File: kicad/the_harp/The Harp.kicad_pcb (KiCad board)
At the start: 4 copper layers, 56 x 94.5 mm, 181 parts, among them J401 PJ-063AH, J402 NMJ6HCD2, J403 NMJ6HCD2, J404 NMJ6HCD2, J405 Bypass FSW, J406 NMJ6HCD2, J407 Hold FSW, K401 G6K-2F-Y, Q401 2N7002, Q402 2N7002, Q403 2N7002, SW101 100-DP6, SW102 100-DP6, SW103 100-DP6, U201 STM32H750VBT6, U301 TPS54202DDC, U302 NCP718ASN500T1G, U401 MCP6001T-I/OT, U501 OPA2348AIDR, U601 THS4522IPW, U701 OPA2365AIDR, U702 OPA1688IDR, Y201 25MHz 9pF

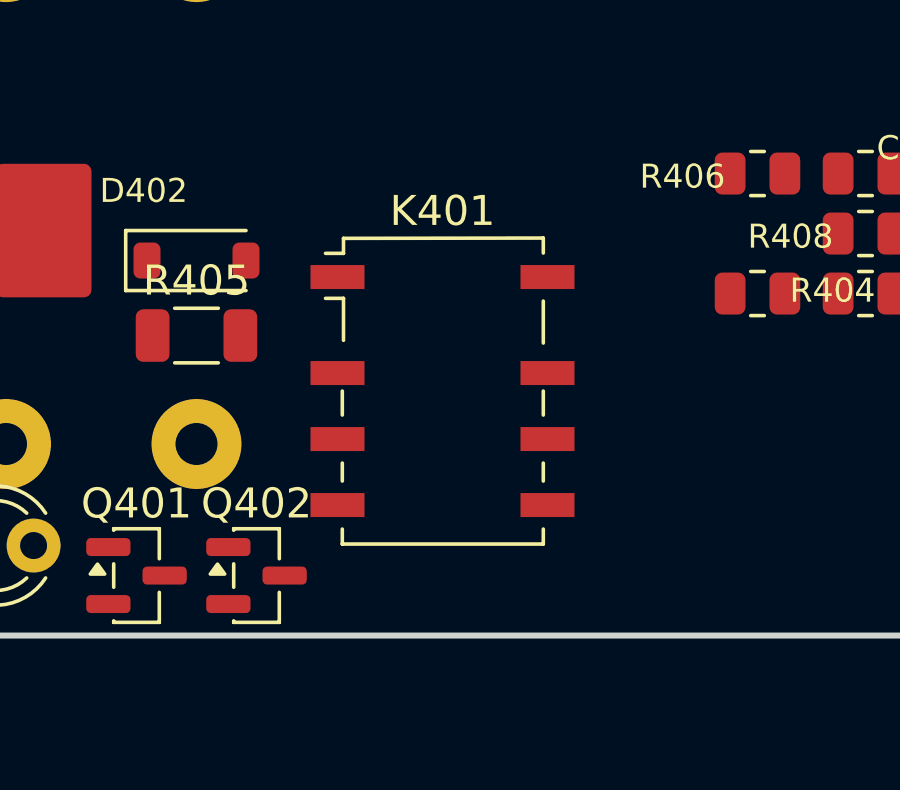
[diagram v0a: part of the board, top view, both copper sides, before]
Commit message: Move K401 out from under the OLED module
K401 from PCB (143.4, 134.85) to (143.9, 137.0), face (-4.6, -32.0): 2.15 mm
towards the heel and 0.5 mm right. Its courtyard now ends 0.5 mm short of the
module edge (Y -26.25), 0.12 mm clear of Q402 and 0.75 mm from the board edge;
a straight 2.5 mm move would have overlapped Q402. No tracks to move (board
unrouted). Drawing and docs updated.

Co-Authored-By: Claude Opus 5.5 <noreply@anthropic.com>
Claude-Session: https://claude.ai/code/session_016hDejPHPgG8auBLMyByYZK
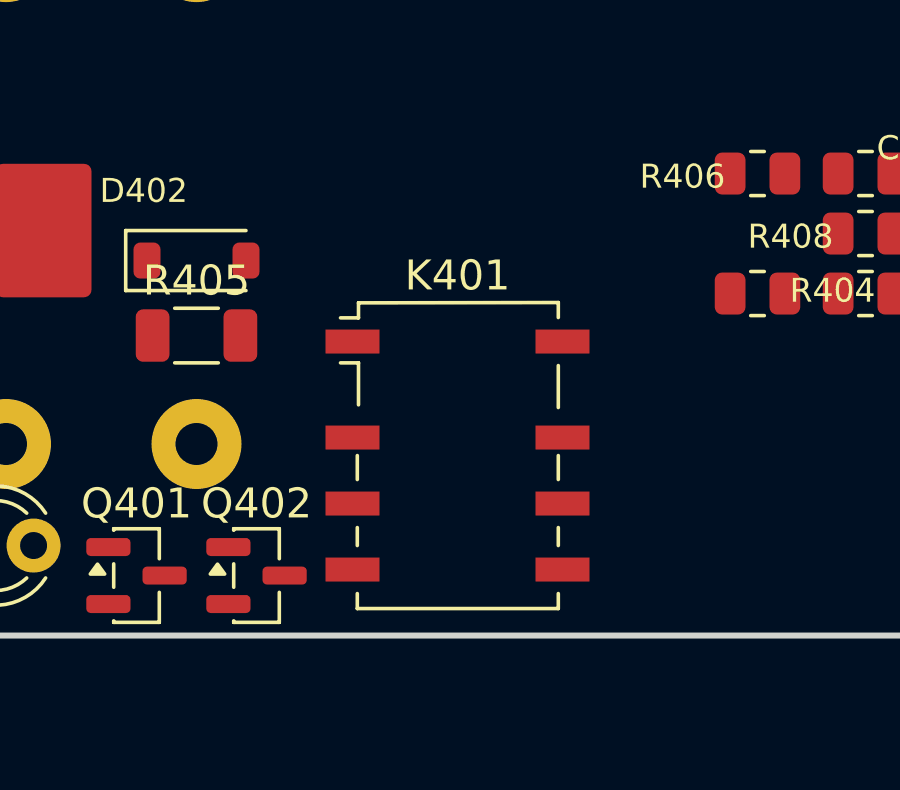
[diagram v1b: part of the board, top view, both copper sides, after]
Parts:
- moved K401 2.21 mm to (143.9, 137.0)
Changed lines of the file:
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@@
 	(footprint "Relay_SMD:Relay_DPDT_Omron_G6K-2F-Y"
 		(layer "F.Cu")
-		(at 143.4 134.85)
+		(at 143.9 137)
 		(descr "Omron G6K-2F-Y relay package http://omronfs.omron.com/en_US/ecb/products/pdf/en-g6k.pdf")
 		(tags "Omron G6K-2F-Y relay")

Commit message: Place J408 on the PCB for the OLED lead
JST SH SM04B-SRSS-TB footprint (KiCad library) added to the board at PCB
(125.0, 122.5), rotation 90, face (-23.5, -17.5): pads in a column at face
X -25.5, cable entry facing the module's pad end. Linked to the schematic
symbol (path /Controls and LEDs/J408) with nets GND, +3V3, OLED_SCL,
OLED_SDA, so Update PCB from Schematic keeps it. Courtyard 1.22 mm from the
board edge and 0.62 mm clear of J405. Drawing and docs updated.

Co-Authored-By: Claude Opus 5.5 <noreply@anthropic.com>
Claude-Session: https://claude.ai/code/session_016hDejPHPgG8auBLMyByYZK
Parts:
- added J408: OLED 0.91 128x32, Connector_JST:JST_SH_SM04B-SRSS-TB_1x04-1MP_P1.00mm_Horizontal, F.Cu at (125.0, 122.5)

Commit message: Sync the PCB to the schematic and park the new parts
Done by script (no KiCad in this session), the equivalent of Update PCB from
Schematic:
- removed D101-D112, R109-R118 (note LEDs) and R502/R503 (parked AINR)
- added 23 footprints: the stereo input parts (R607-R612, C611-C618,
  R720-R722, C708, C709, D407), C104, and IC501 / U202, which were missing
  from the board; library footprints cloned from this board or the
  Timekeeper's, rotation normalised, fresh UUIDs, linked to their symbols
- updated values and pad nets on 13 footprints (U601 channel B, U701B,
  IC501 inputs, ADC_L nets, J402 ring, U201 PB6/PB7 and freed PD0-PD11,
  R107/R108 now 4.7k pull-ups)
Checked: all 181 footprints match harp_spec.py pin by pin, every path
points at a schematic symbol. New parts are parked off-board at face X
132-160 beside the other parked groups.

Co-Authored-By: Claude Opus 5.5 <noreply@anthropic.com>
Claude-Session: https://claude.ai/code/session_016hDejPHPgG8auBLMyByYZK
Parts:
- removed D101, D102, D103, D104, D105, D106, D107, D108, D109, D110, D111, D112: LED, LED_SMD:LED_0603_1608Metric
- removed R109, R110, R111, R112, R113, R114, R115, R116, R117, R118, R502, R503: 1k, Resistor_SMD:R_0603_1608Metric
- added C104: 100n, Capacitor_SMD:C_0603_1608Metric, F.Cu at (280.5, 80.0)
- added C611: 100p, Capacitor_SMD:C_0603_1608Metric, F.Cu at (280.5, 132.0)
- added C612: 100p, Capacitor_SMD:C_0603_1608Metric, F.Cu at (284.5, 132.0)
- added C613: 1n, Capacitor_SMD:C_0603_1608Metric, F.Cu at (288.5, 132.0)
- added C614: 1n, Capacitor_SMD:C_0603_1608Metric, F.Cu at (292.5, 132.0)
- added C615: 2.7n, Capacitor_SMD:C_0603_1608Metric, F.Cu at (296.5, 132.0)
- added C616: 100p, Capacitor_SMD:C_0603_1608Metric, F.Cu at (300.5, 132.0)
- added C617: 100p, Capacitor_SMD:C_0603_1608Metric, F.Cu at (304.5, 132.0)
- added C618: 100n, Capacitor_SMD:C_0603_1608Metric, F.Cu at (308.5, 132.0)
- added C708: 100n, Capacitor_SMD:C_1206_3216Metric, F.Cu at (293.5, 115.0)
- added C709: 220p, Capacitor_SMD:C_0603_1608Metric, F.Cu at (298.5, 115.0)
- added D407: PESD5V0U1BB,115, Diode_SMD:D_SOD-523, F.Cu at (280.5, 105.0)
- added IC501: AK4621EF, Audio_Module:SOP65P760X150-30N, F.Cu at (288.5, 150.0)
- added R607: 1k, Resistor_SMD:R_0603_1608Metric, F.Cu at (280.5, 127.0)
- added R608: 1.05k, Resistor_SMD:R_0603_1608Metric, F.Cu at (284.5, 127.0)
- added R609: 620, Resistor_SMD:R_0603_1608Metric, F.Cu at (288.5, 127.0)
- added R610: 620, Resistor_SMD:R_0603_1608Metric, F.Cu at (292.5, 127.0)
- added R611: 40.2, Resistor_SMD:R_0603_1608Metric, F.Cu at (296.5, 127.0)
- added R612: 40.2, Resistor_SMD:R_0603_1608Metric, F.Cu at (300.5, 127.0)
- added R720: 1M, Resistor_SMD:R_0603_1608Metric, F.Cu at (280.5, 115.0)
- added R721: 1M, Resistor_SMD:R_0603_1608Metric, F.Cu at (284.5, 115.0)
- added R722: 49.9, Resistor_SMD:R_0603_1608Metric, F.Cu at (288.5, 115.0)
- added U202: W25Q128JVSIQ, Package_SO:SOIC-8_5.23x5.23mm_P1.27mm, F.Cu at (286.5, 95.0)
- R107, R108: value 1k -> 4.7k
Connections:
- net /Analog In and Out/U701B_OUT renamed /Analog In and Out/IN_BUF_OUT_R
- net ADC_N renamed ADC_L_N
- net ADC_P renamed ADC_L_P
- J402 pad R: GND -> IN_R
- R107 pad 1: NOTE_C -> +3V3
- R107 pad 2: /Controls and LEDs/NOTE_C_A -> OLED_SCL
- R108 pad 1: NOTE_Cs -> +3V3
- R108 pad 2: /Controls and LEDs/NOTE_Cs_A -> OLED_SDA
- U201 pad 55: NOTE_Gs -> unconnected-(U201-PD8-Pad55)
- U201 pad 56: NOTE_A -> unconnected-(U201-PD9-Pad56)
- U201 pad 57: NOTE_As -> unconnected-(U201-PD10-Pad57)
- U201 pad 58: NOTE_B -> unconnected-(U201-PD11-Pad58)
- U201 pad 81: NOTE_C -> unconnected-(U201-PD0-Pad81)
- U201 pad 82: NOTE_Cs -> unconnected-(U201-PD1-Pad82)
- U201 pad 83: NOTE_D -> unconnected-(U201-PD2-Pad83)
- U201 pad 84: NOTE_Ds -> unconnected-(U201-PD3-Pad84)
- U201 pad 85: NOTE_E -> unconnected-(U201-PD4-Pad85)
- U201 pad 86: NOTE_F -> unconnected-(U201-PD5-Pad86)
- U201 pad 87: NOTE_Fs -> unconnected-(U201-PD6-Pad87)
- U201 pad 88: NOTE_G -> unconnected-(U201-PD7-Pad88)
- U201 pad 92: unconnected-(U201-PB6-Pad92) -> OLED_SCL
- U201 pad 93: unconnected-(U201-PB7-Pad93) -> OLED_SDA
- U601 pad 10: unconnected-(U601B-OUTP-Pad10) -> /ADC Driver/FDB_OUTP
- U601 pad 11: unconnected-(U601B-OUTN-Pad11) -> /ADC Driver/FDB_OUTN
- U601 pad 5: GND -> +5V
- U601 pad 6: GND -> /ADC Driver/FDB_INP
- U601 pad 7: GND -> /ADC Driver/FDB_INN
- U601 pad 8: GND -> VCOM_B
- U701 pad 5: VCOM_A -> /Analog In and Out/IN_AC_R

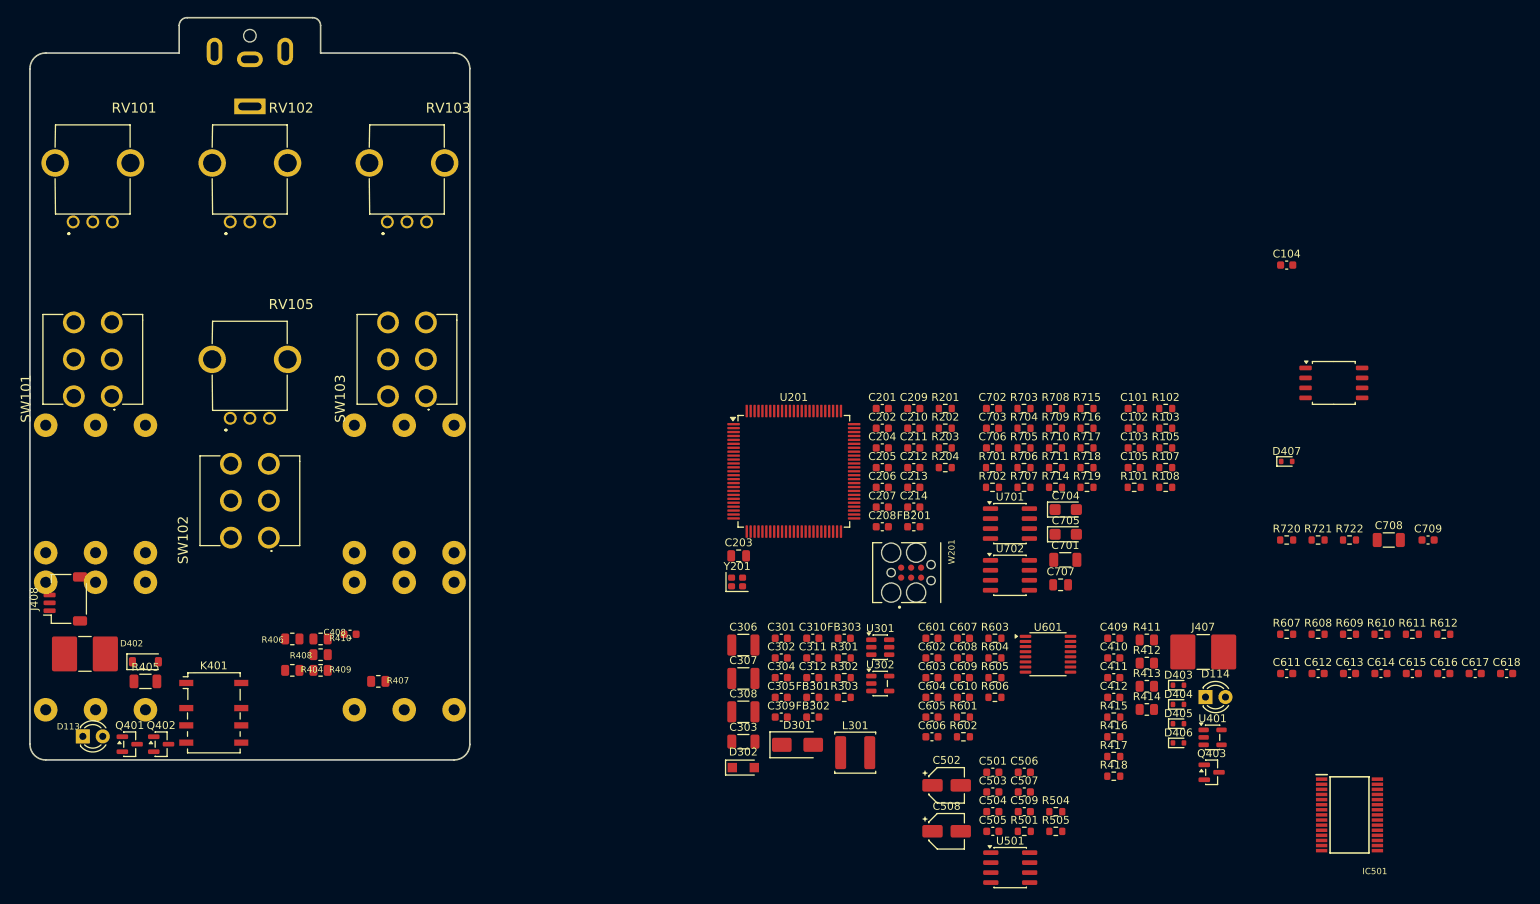
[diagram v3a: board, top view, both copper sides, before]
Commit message: Place every part on the board (scripted), Plan A go/no-go
All 181 footprints placed on the top side by a greedy, zoned placer
(scripts/pcb_placement/): no courtyard overlaps, everything inside the
outline, nothing tall under the OLED module, about 68 % courtyard fill.

The LQFP-100 fits in only one place, the lower centre between the lower
jacks' pin rows (0, -21.5), so the zoning was adapted round it: relay next
to IN, input buffers lower right, ADC driver left middle, codec and output
stages between the pot rows, buck and LDO in the top band. J408 moved to
(-21.75, -22.0): its first position sat on J403's rear pins.

Verdict in docs/pcb-plan.md "Placement": Plan A fits, but the right-channel
ADC driver network, the codec-to-MCU SAI lines and the input path need
rework by hand before routing. Placement drawing, OLED drawing, brief,
design report and READMEs updated.

Co-Authored-By: Claude Opus 5.5 <noreply@anthropic.com>
Claude-Session: https://claude.ai/code/session_016hDejPHPgG8auBLMyByYZK
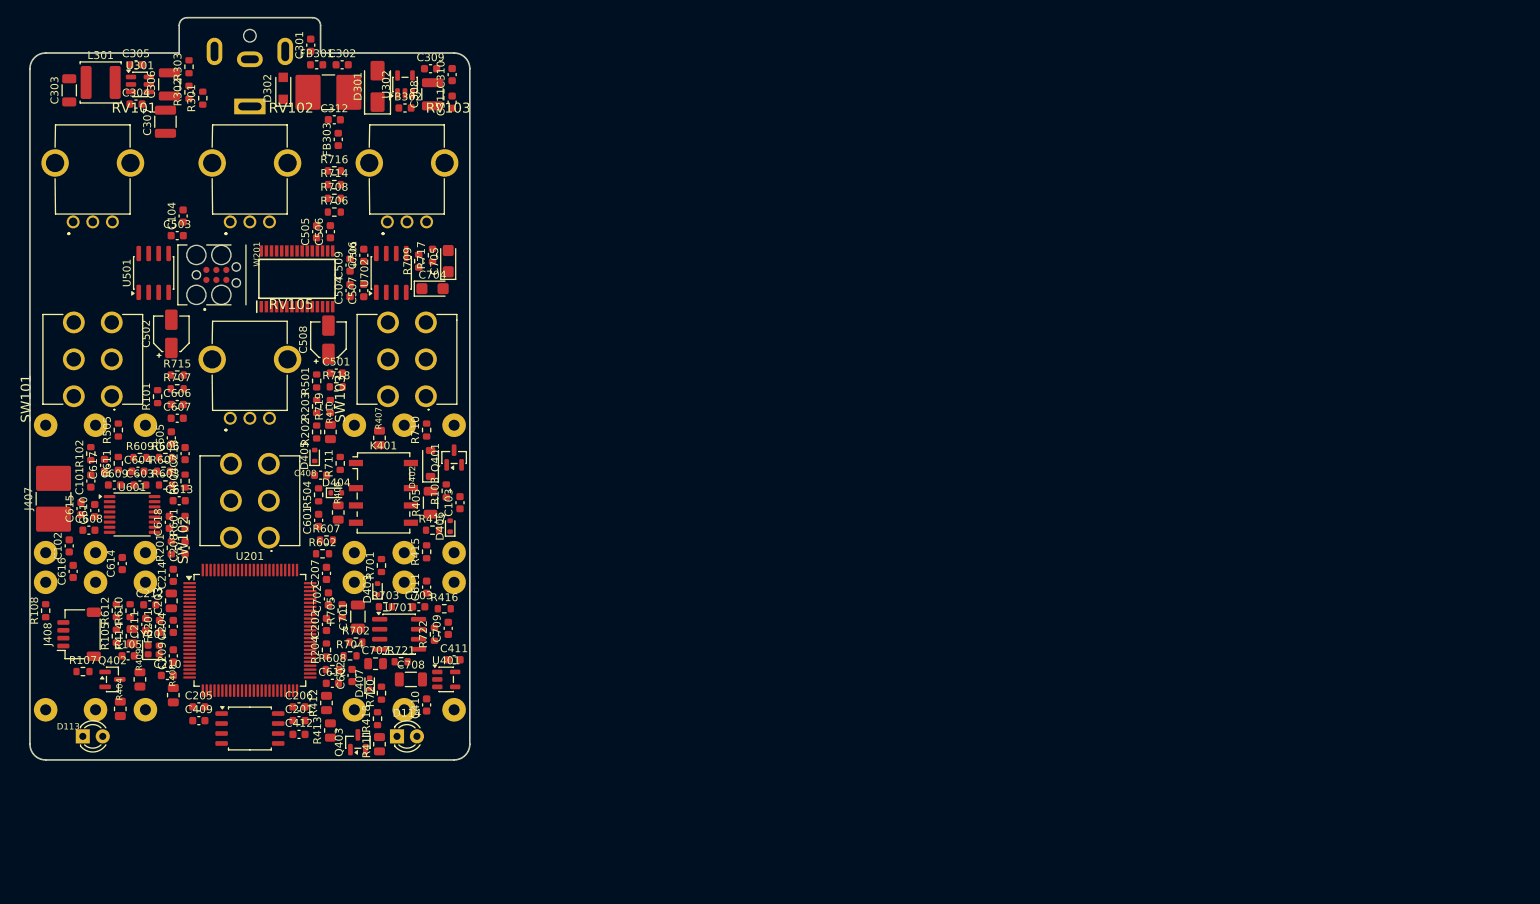
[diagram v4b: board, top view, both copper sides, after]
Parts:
- moved C617 176.5 mm to (130.0, 105.5), turned to 90 degrees
- moved C616 175.0 mm to (126.0, 119.0), turned to 90 degrees
- moved C618 171.3 mm to (138.2, 112.8), turned to 90 degrees
- moved C615 170.8 mm to (127.0, 111.0), turned to 90 degrees
- moved R612 169.0 mm to (131.5, 124.0), turned to 90 degrees
- moved R611 166.2 mm to (131.8, 105.2), turned to 90 degrees
- moved C614 160.9 mm to (132.2, 118.0), turned to 90 degrees
- moved R610 159.3 mm to (133.2, 124.0), turned to 90 degrees
- moved R609 155.6 mm to (134.5, 104.5)
- moved C613 150.6 mm to (139.5, 110.0)
- moved IC501 150.4 mm to (154.5, 81.8), turned to 90 degrees
- moved J407 147.7 mm to (123.5, 109.8), turned to 90 degrees
- moved U202 144.8 mm to (148.5, 139.0)
- moved R108 143.5 mm to (122.5, 124.0), turned to 90 degrees
- moved C104 140.6 mm to (140.0, 73.8), turned to 90 degrees
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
